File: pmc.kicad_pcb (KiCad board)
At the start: 6 copper layers, 47 x 45.1 mm, 142 parts, among them M1 LM46001, M2 TPS61040, M3 STM32F4XX, M4 REF30XX, M5 TPS736XX, M6 SN65HVD23X, M7 UCC27211A, M8 UCC27211A, M9 UCC27211A, P1 BOOT, P10 CONN4, P11 DEBUG, P2 PWM, P3 HALL, P4 SPI, P5 CAN, P6 CONN4, P7 CONN4, P8 CONN4, P9 CONN4, Q1 BC857C, Q2 IPT007N06N, Q3 IPT007N06N, Q4 IPT007N06N, Q5 IPT007N06N, Q6 IPT007N06N, Q7 IPT007N06N, U1 AD8539, U2 AD8539, U3 AD8417, U4 AD8417

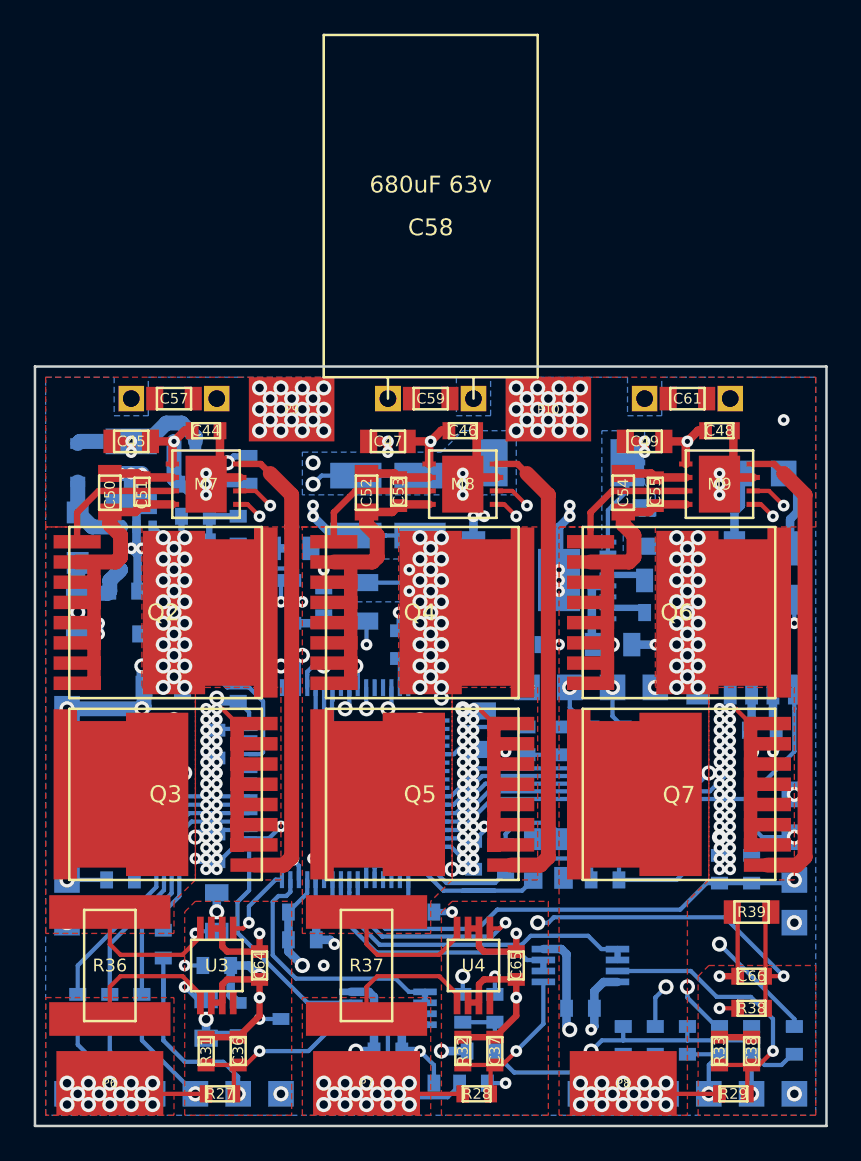
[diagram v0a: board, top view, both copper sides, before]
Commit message: Small fixes in schematic and pcb.
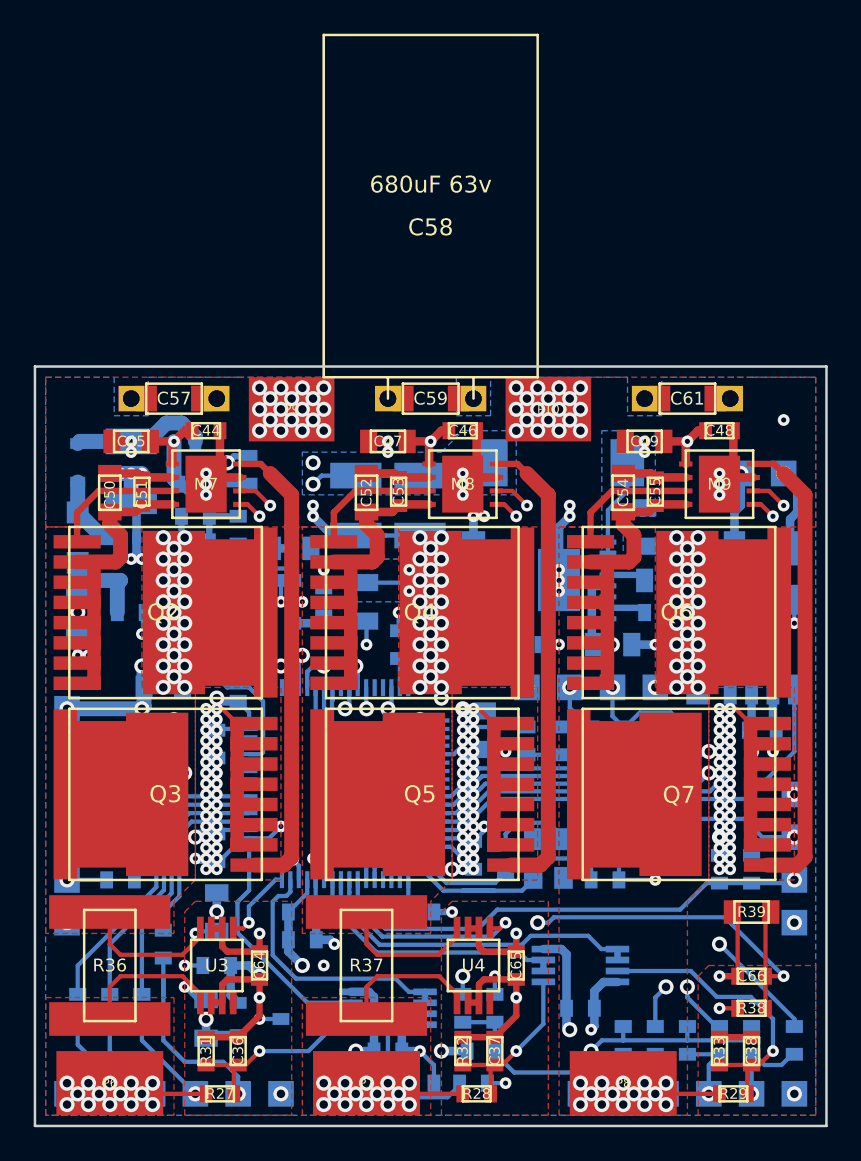
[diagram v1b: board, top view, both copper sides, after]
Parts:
- removed C29: 100nF 25v, foot:SM0603
- added R43: 10K, foot:SM0603, B.Cu at (99.7, 89.5)
- added R44: 10K, foot:SM0603, B.Cu at (101.6, 89.5)
- C11: value 100nF 15v -> 100nF 25v
- C32, C33, C34: value 100nF -> 100nF 25v
- C57, C59, C61: value 100nF 100v -> 2.2uF 100v; footprint foot:SM0805 -> foot:SM1206
- M3: value STM32F4XX -> STM32F405RG
- M4: value REF30XX -> REF3033
- M5: value TPS736XX -> TPS73633
- M6: value SN65HVD23X -> SN65HVD233
- moved R16 6.63 mm to (101.6, 95.9), turned to 90 degrees
- moved C4 1.35 mm to (68.6, 81.9)
- moved M2 0.63 mm to (68.9, 78.7)
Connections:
- net BEMF_A renamed VOLTAGE_A
- net BEMF_B renamed VOLTAGE_B
- net BEMF_C renamed VOLTAGE_C
- net SENSOR_A renamed CURRENT_A
- net SENSOR_B renamed CURRENT_B
- net SENSOR_U renamed VOLTAGE_U
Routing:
- net PWM_INB: track 2.61 -> 7.13 mm
- net PWM_INA: track 2.95 -> 7.44 mm
- net GND: track 263.0 -> 259.5 mm
- net +3.3V: track 59.3 -> 62.6 mm, vias 17 -> 18
- net BOOT: track 25.6 -> 28.6 mm
- net +36V: track 128.7 -> 131.4 mm
- net +5V: track 52.0 -> 52.7 mm
- net Net-(M6-Pad7): vias 0 -> 1
- net Net-(M6-Pad6): vias 0 -> 1
- added copper zone on In1.Cu, net +36V
- added copper zone on In2.Cu, net GND
- added copper zone on In1.Cu, net TERMINAL_A
- added copper zone on In2.Cu, net TERMINAL_A
- added copper zone on In1.Cu, net TERMINAL_B
- added copper zone on In2.Cu, net TERMINAL_B
- added copper zone on In1.Cu, net TERMINAL_C
- added copper zone on In2.Cu, net TERMINAL_C

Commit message: Minor fixing.
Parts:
- moved P5 0.63 mm to (106.0, 73.0)
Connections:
- net PWM_INA renamed I2C_SCL
- net PWM_INB renamed I2C_SDA
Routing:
- net Net-(M6-Pad6): track 8.07 -> 8.71 mm, vias 1 -> 0
- net Net-(M6-Pad7): track 8.80 -> 9.06 mm, vias 1 -> 0

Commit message: Fixed SilkS layers.
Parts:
- moved R39 1.89 mm to (104.0, 101.0)
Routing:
- net GND: track 259.5 -> 258.4 mm
- net PCB_NTC: track 38.3 -> 37.8 mm
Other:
- board text added: "+3.3V"
- board text added: "+40V"
- board text added: "+5V"
- board text added: "A"
- board text added: "B"
- board text added: "BOOT"
- board text added: "C"
- board text added: "CAN"
- board text added: "GND"
- board text added: "H"
- board text added: "L"
- board text added: "MISO"
- board text added: "MOSI"
- board text added: "NSS"
- board text added: "NTC"
- board text added: "PMC (rev4)"
- board text added: "RX"
- board text added: "SCK"
- board text added: "SCL"
- board text added: "SDA"
- board text added: "SWCLK"
- board text added: "SWDIO"
- board text added: "TX"
- board text added: "term. C"
